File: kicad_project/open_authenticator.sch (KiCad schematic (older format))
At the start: 67 parts, among them IC1 TPS22919DCKR, J1 Conn_01x02_Female, J2 TYPE-C-31-M-17, J3 Conn_01x02_Female, P1 SSD1306_ribbon, Q1 DMP2305U-7, SW1 UP, SW2 DOWN, SW3 BOOT/SELECT, SW4 RESET, SW5 POWER SWITCH, U1 ESP32-WROOM-32, U2 DS3231M, U3 MCP73831-2-OT, U4 TPS63001

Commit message: Added lipo battery connector to schematics
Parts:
- removed J3: Conn_01x02_Female, Connector_PinHeader_1.27mm:PinHeader_1x02_P1.27mm_Vertical, symbol Connector:Conn_01x02_Female
- added J3: S2B-PH-SM4-TB(LF)(SN), jst-ph-2-pin-connector:JST_S2B-PH-SM4-TB(LF)(SN), symbol S2B-PH-SM4-TB_LF__SN_:S2B-PH-SM4-TB(LF)(SN)
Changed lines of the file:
@@
-$EndComp
-$Comp
-L power:GND #PWR031
-U 1 1 5FC0BC1F
-P 12450 2150
-F 0 "#PWR031" H 12450 1900 50  0001 C CNN
-F 1 "GND" H 12455 1977 50  0000 C CNN
-F 2 "" H 12450 2150 50  0001 C CNN
-F 3 "" H 12450 2150 50  0001 C CNN
-	1    12450 2150
-	1    0    0    -1
 $EndComp
 $Comp
 L power:+BATT #PWR032
 U 1 1 5FC0BFDD
-P 12950 2150
-F 0 "#PWR032" H 12950 2000 50  0001 C CNN
-F 1 "+BATT" H 12965 2323 50  0000 C CNN
-F 2 "" H 12950 2150 50  0001 C CNN
-F 3 "" H 12950 2150 50  0001 C CNN
-	1    12950 2150
+P 12450 2050
+F 0 "#PWR032" H 12450 1900 50  0001 C CNN
+F 1 "+BATT" H 12465 2223 50  0000 C CNN
+F 2 "" H 12450 2050 50  0001 C CNN
+F 3 "" H 12450 2050 50  0001 C CNN
+	1    12450 2050
 	-1   0    0    1
 $EndComp
@@
 Text Label 10750 9700 1    39   ~ 0
 V_INPUT
-Wire Wire Line
-	12450 2150 12650 2150
-Wire Wire Line
-	12750 2150 12950 2150
 Wire Wire Line
 	8800 3500 8800 3100
@@
 Wire Wire Line
 	11850 5800 11450 5800
-$Comp
-L Connector:Conn_01x02_Female J3
-U 1 1 5FBD9746
-P 12650 1100
-F 0 "J3" V 12588 912 50  0000 R CNN
-F 1 "Conn_01x02_Female" V 12497 912 50  0000 R CNN
-F 2 "Connector_PinHeader_1.27mm:PinHeader_1x02_P1.27mm_Vertical" H 12650 1100 50  0001 C CNN
-F 3 "~" H 12650 1100 50  0001 C CNN
-	1    12650 1100
-	0    -1   -1   0
-$EndComp
-Wire Wire Line
-	12650 1300 12650 2150
-Wire Wire Line
-	12750 1300 12750 2150
 $Comp
 L open_authenticator-rescue:C-Device-esp_2fa_board_design-rescue-esp_2fa_board_design-rescue-open_authenticator-rescue C2
@@
 Wire Wire Line
 	8850 10350 8850 10650
+$Comp
+L S2B-PH-SM4-TB_LF__SN_:S2B-PH-SM4-TB(LF)(SN) J3
+U 1 1 6009EEC8
+P 12550 1650
+F 0 "J3" V 12538 1322 50  0000 R CNN
+F 1 "S2B-PH-SM4-TB(LF)(SN)" V 12447 1322 50  0000 R CNN
+F 2 "jst-ph-2-pin-connector:JST_S2B-PH-SM4-TB(LF)(SN)" H 12550 1650 50  0001 L BNN
+F 3 "" H 12550 1650 50  0001 L BNN
+F 4 "JST" H 12550 1650 50  0001 L BNN "MANUFACTURER"
+F 5 "Manufacturer Recommendation" H 12550 1650 50  0001 L BNN "STANDARD"
+	1    12550 1650
+	0    -1   -1   0
+$EndComp
+$Comp
+L power:GND #PWR031
+U 1 1 5FC0BC1F
+P 12650 2050
+F 0 "#PWR031" H 12650 1800 50  0001 C CNN
+F 1 "GND" H 12655 1877 50  0000 C CNN
+F 2 "" H 12650 2050 50  0001 C CNN
+F 3 "" H 12650 2050 50  0001 C CNN
+	1    12650 2050
+	1    0    0    -1
+$EndComp
+Wire Wire Line
+	12550 1950 12650 1950
+Wire Wire Line
+	12650 2050 12650 1950
+Connection ~ 12650 1950
+Wire Wire Line
+	12650 1950 12750 1950
+Wire Wire Line
+	12450 1950 12450 2050
 $EndSCHEMATC

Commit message: Updated schematics to include info about battery
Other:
- note added: "Connect 4.2V rated 1C Lithium \nPolymer Battery. Preferably 402025 \nsized 300mAh battery\n\nSize: 20mmx20mmx4mm"
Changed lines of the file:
@@
 Wire Wire Line
 	12450 1950 12450 2050
+Text Notes 12250 1350 0    50   ~ 0
+Connect 4.2V rated 1C Lithium \nPolymer Battery. Preferably 402025 \nsized 300mAh battery\n\nSize: 20mmx20mmx4mm
 $EndSCHEMATC

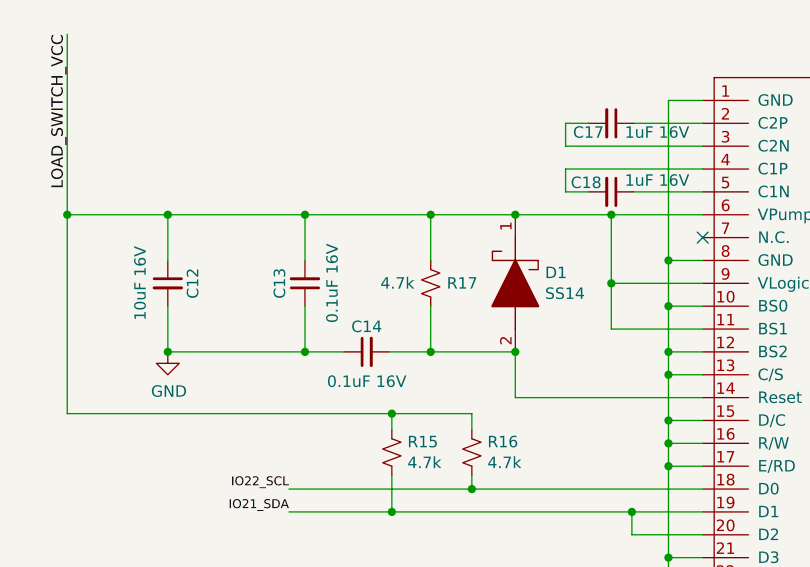
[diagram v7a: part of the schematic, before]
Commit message: Changed R17 from 4.7k -> 310k in schematics to fix OLED Reset Issue
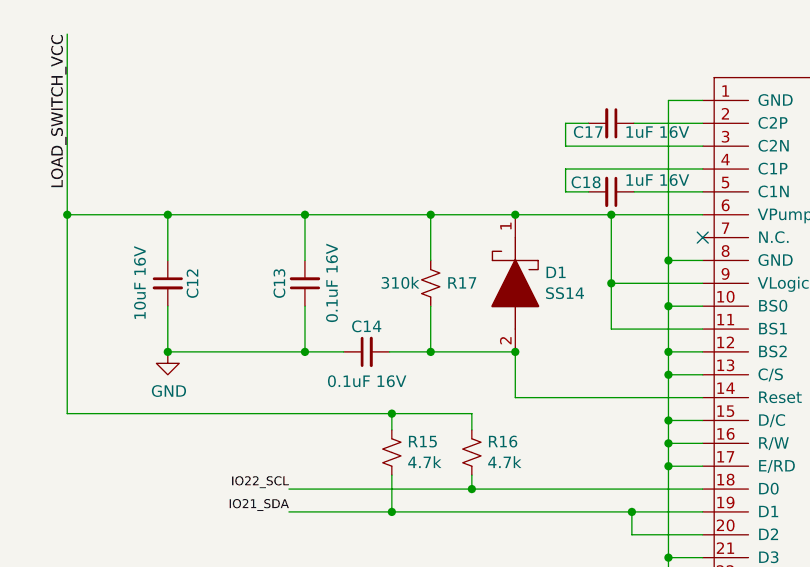
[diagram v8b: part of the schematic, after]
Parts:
- R17: value 4.7k -> 310k
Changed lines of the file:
@@
 P 8410 5950
 F 0 "R17" H 8480 5950 50  0000 L CNN
-F 1 "4.7k" H 8190 5950 50  0000 L CNN
+F 1 "310k" H 8190 5950 50  0000 L CNN
 F 2 "Resistor_SMD:R_0603_1608Metric" H 8410 5950 50  0001 C CNN
 F 3 "~" H 8410 5950 50  0001 C CNN
